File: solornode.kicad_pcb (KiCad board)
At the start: 2 copper layers, 35.9 x 42.4 mm, 85 parts, among them J1 Conn_01x06, J2 Conn_01x02, J3 Conn_01x02, J4 Conn_01x02, Q1 AO3400, Q4 S8550, Q5 S8050, SW1 3*4*2mm, U1 LM358, U2 OC5864, U3 PY32F003F18U6TR, U4 MAX485E, U5 SGM2033-3.3

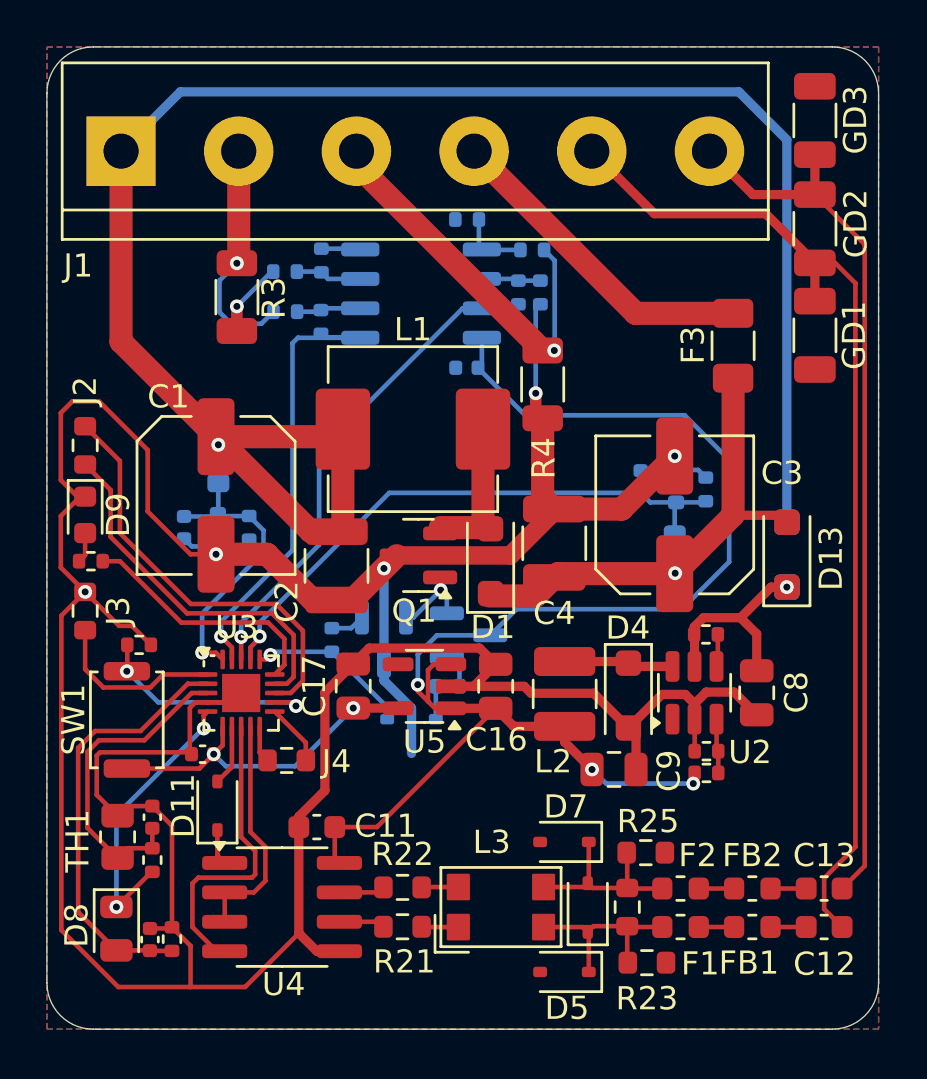
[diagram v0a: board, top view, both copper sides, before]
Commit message: 改进GND连接，添加一处实心连接覆铜，自定义通孔NetTie
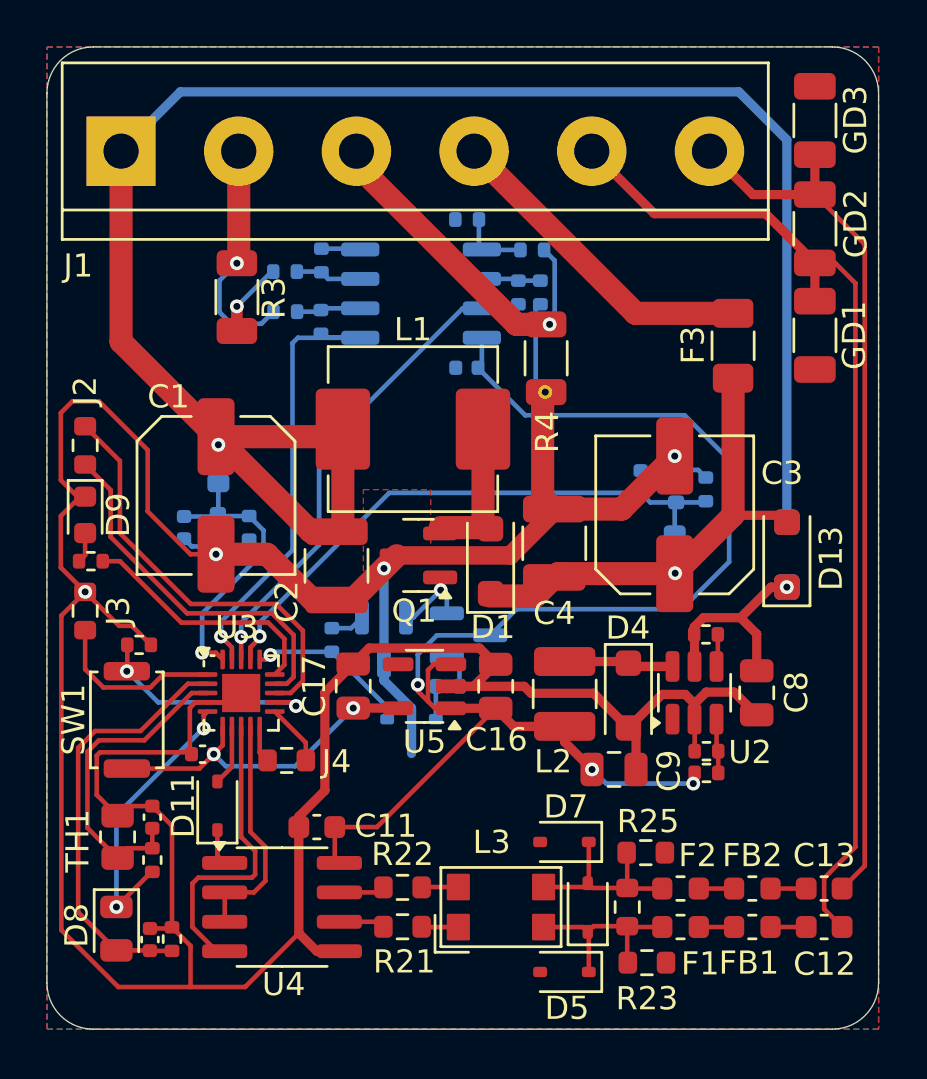
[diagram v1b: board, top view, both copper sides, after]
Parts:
- NT1: footprint NetTie:NetTie-2_SMD_Pad0.5mm -> ProjectLibrary:NetTie-2_VIA_Pad0.6_0.3mm
- moved R4 1.14 mm to (134.2, 70.3)
- moved NT1 0.69 mm to (134.1, 71.8)
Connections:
- NT1 pad 1: /BUS_Is -> GND
- NT1 pad 2: GND -> /BUS_Is
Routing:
- net /BUS-: track 16.5 -> 15.3 mm
- net GND: track 160.9 -> 162.1 mm
- net /BUS_Is: track 3.99 -> 4.11 mm, vias 1 -> 0
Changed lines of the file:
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@@
 		)
 	)
-	(footprint "NetTie:NetTie-2_SMD_Pad0.5mm"
+	(footprint "ProjectLibrary:NetTie-2_VIA_Pad0.6_0.3mm"
 		(layer "F.Cu")
-		(at 133.7 72.35 -90)
+		(at 134.11 71.8 -90)
 		(descr "Net tie, 2 pin, 0.5mm square SMD pads")
 		(tags "net tie")
 		(property "Reference" "NT1"
-			(at 0 -1.2 90)
+			(at 0 -1.2 -90)
 			(layer "F.SilkS")
 			(hide yes)
@@
 		)
 		(property "Value" "NetTie_2"
-			(at 0 1.2 90)
+			(at 0 1.2 -90)
 			(layer "F.Fab")
 			(hide yes)
@@
 			)
 		)
-		(property "Footprint" "NetTie:NetTie-2_SMD_Pad0.5mm"
+		(property "Footprint" "ProjectLibrary:NetTie-2_VIA_Pad0.6_0.3mm"
 			(at 0 0 -90)
 			(unlocked yes)
@@
 		(attr exclude_from_pos_files exclude_from_bom allow_missing_courtyard)
 		(net_tie_pad_groups "1, 2")
-		(fp_poly
-			(pts
-				(xy -0.5 -0.25) (xy 0.5 -0.25) (xy 0.5 0.25) (xy -0.5 0.25)
-			)
-			(stroke
-				(width 0)
-				(type solid)
+		(pad "1" thru_hole circle
+			(at 0 0 270)
+			(size 0.6 0.6)
+			(drill 0.3)
+			(layers "*.Cu" "*.Mask" "In1.Cu" "In2.Cu" "In3.Cu" "In4.Cu" "In5.Cu" "In6.Cu"
+				"In7.Cu" "In8.Cu" "In9.Cu" "In10.Cu" "In11.Cu" "In12.Cu" "In13.Cu" "In14.Cu"
+				"In15.Cu" "In16.Cu" "In17.Cu" "In18.Cu" "In19.Cu" "In20.Cu" "In21.Cu"
+				"In22.Cu" "In23.Cu" "In24.Cu" "In25.Cu" "In26.Cu" "In27.Cu" "In28.Cu"
+				"In29.Cu" "In30.Cu"
 			)
-			(fill solid)
-			(layer "F.Cu")
-		)
-		(pad "1" smd circle
-			(at -0.5 0 270)
-			(size 0.5 0.5)
-			(layers "F.Cu")
-			(net 24 "/BUS_Is")
+			(remove_unused_layers no)
+			(net 1 "GND")
 			(pinfunction "1")
 			(pintype "passive")
 		)
 		(pad "2" smd circle
-			(at 0.5 0 270)
-			(size 0.5 0.5)
-			(layers "F.Cu")
-			(net 1 "GND")
+			(at 0 0 270)
+			(size 0.6 0.6)
+			(layers "B.Cu")
+			(net 24 "/BUS_Is")
 			(pinfunction "2")
 			(pintype "passive")
@@
 	(footprint "Resistor_SMD:R_1206_3216Metric"
 		(layer "F.Cu")
-		(at 134 71.4675 90)
+		(at 134.15 70.34 90)
 		(descr "Resistor SMD 1206 (3216 Metric), square (rectangular) end terminal, IPC_7351 nominal, (Body size source: IPC-SM-782 page 72, https://www.pcb-3d.com/wordpress/wp-content/uploads/ipc-sm-782a_amendment_1_and_2.pdf), generated with kicad-footprint-generator")
 		(tags "resistor")
@@
 	)
 	(segment
+		(start 134 71.9525)
+		(end 134 76.35)
+		(width 1)
+		(layer "F.Cu")
+		(net 1)
+	)
+	(segment
 		(start 117.05 94.9525)
 		(end 117.95 94.9525)
@@
 	)
 	(segment
+		(start 134.15 71.8025)
+		(end 134 71.9525)
+		(width 1)
+		(layer "F.Cu")
+		(net 1)
+	)
+	(segment
 		(start 120.585 85.19)
 		(end 120.985 84.79)
@@
 	)
 	(segment
+		(start 134 76.35)
+		(end 134.5 76.85)
+		(width 1)
+		(layer "F.Cu")
+		(net 1)
+	)
+	(segment
 		(start 116.0675 89.67)
 		(end 115.65 90.0875)
@@
 	)
 	(segment
-		(start 134 76.35)
-		(end 134.5 76.85)
-		(width 1)
-		(layer "F.Cu")
-		(net 1)
-	)
-	(segment
 		(start 140.555 85.9175)
 		(end 140.555 85.255001)
@@
 	)
 	(segment
-		(start 134 72.93)
-		(end 134 76.35)
-		(width 1)
-		(layer "F.Cu")
-		(net 1)
-	)
-	(segment
 		(start 139.15 84.85)
 		(end 137.7 86.3)
@@
 		(net 23)
 	)
-	(via
-		(at 133.7 71.85)
-		(size 0.6)
-		(drill 0.3)
-		(layers "F.Cu" "B.Cu")
+	(segment
+		(start 133.7 71.39)
+		(end 133.7 68.21)
+		(width 0.2)
+		(layer "B.Cu")
 		(net 24)
 	)
 	(segment
-		(start 133.9 68.01)
-		(end 133.7 68.21)
+		(start 134.11 71.8)
+		(end 133.7 71.39)
 		(width 0.2)
 		(layer "B.Cu")
@@
 	(segment
 		(start 133.7 68.21)
-		(end 133.7 71.85)
+		(end 133.9 68.01)
 		(width 0.2)
 		(layer "B.Cu")
@@
 	)
 	(segment
-		(start 134 70.005)
+		(start 125.96 61.965)
+		(end 125.96 61.4)
+		(width 1)
+		(layer "F.Cu")
+		(net 31)
+	)
+	(segment
+		(start 132.8725 68.8775)
 		(end 125.96 61.965)
 		(width 1)
@@
 	)
 	(segment
-		(start 125.96 61.965)
-		(end 125.96 61.4)
+		(start 134.3 68.8775)
+		(end 132.8725 68.8775)
 		(width 1)
 		(layer "F.Cu")
@@
 	)
 	(via
-		(at 134.5 70.005)
+		(at 134.3 68.8775)
 		(size 0.6)
 		(drill 0.3)
@@
 	)
 	(segment
-		(start 134.52 69.985)
-		(end 134.52 66.125)
+		(start 134.3 68.8775)
+		(end 134.52 68.6575)
 		(width 0.2)
 		(layer "B.Cu")
@@
 	)
 	(segment
-		(start 134.5 70.005)
-		(end 134.52 69.985)
+		(start 134.52 68.6575)
+		(end 134.52 66.125)
 		(width 0.2)
 		(layer "B.Cu")
@@
 		(net 1)
 		(net_name "GND")
+		(layer "F.Cu")
+		(hatch edge 0.5)
+		(priority 1)
+		(connect_pads yes
+			(clearance 0.5)
+		)
+		(min_thickness 0.25)
+		(filled_areas_thickness no)
+		(fill
+			(thermal_gap 0.5)
+			(thermal_bridge_width 0.5)
+		)
+		(polygon
+			(pts
+				(xy 126.26 76.01) (xy 129.17 76.01) (xy 129.17 78.99) (xy 126.26 79.52)
+			)
+		)
+	)
+	(zone
+		(net 1)
+		(net_name "GND")
 		(layers "F.Cu" "B.Cu")
 		(hatch edge 0.5)
@@
 			"b830b06e-fbac-4581-8a56-22dc22e87084" "ba1f4f5e-80dd-4566-8626-b2ffeb4854c5"
 			"bb377057-8535-4cfd-9200-875104dc9782" "bc114b9e-2d28-4ff4-b9b3-e5020ca9fe90"
-			"c4519f8f-6f26-4239-bd34-729a9c87b534" "cc70d371-8e1c-4e16-b46e-346a7447f6c0"
-			"d414d630-ed2d-4de0-a73b-ad1c64c80433" "d8507c6e-e514-4256-86ee-3f98cede7189"
-			"f882931f-e173-4b64-a534-4f37fa19a90f"
+			"c4519f8f-6f26-4239-bd34-729a9c87b534" "d8507c6e-e514-4256-86ee-3f98cede7189"
 		)
 	)
